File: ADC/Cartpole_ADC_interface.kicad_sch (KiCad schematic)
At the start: 9 parts, among them J1 Socket for JST XH, J2 Socket for potentiometer leads

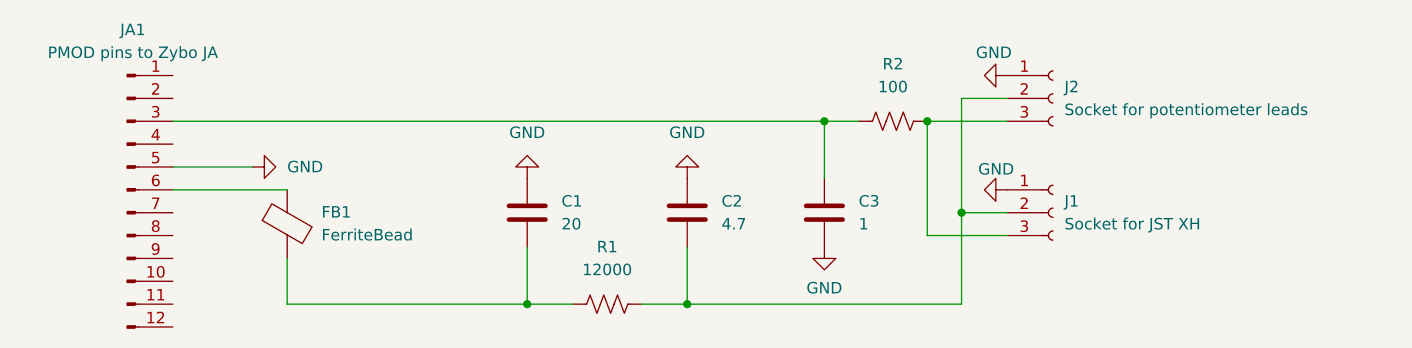
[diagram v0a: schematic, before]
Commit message: Fit left size of ADC interface board to the PMOD spec
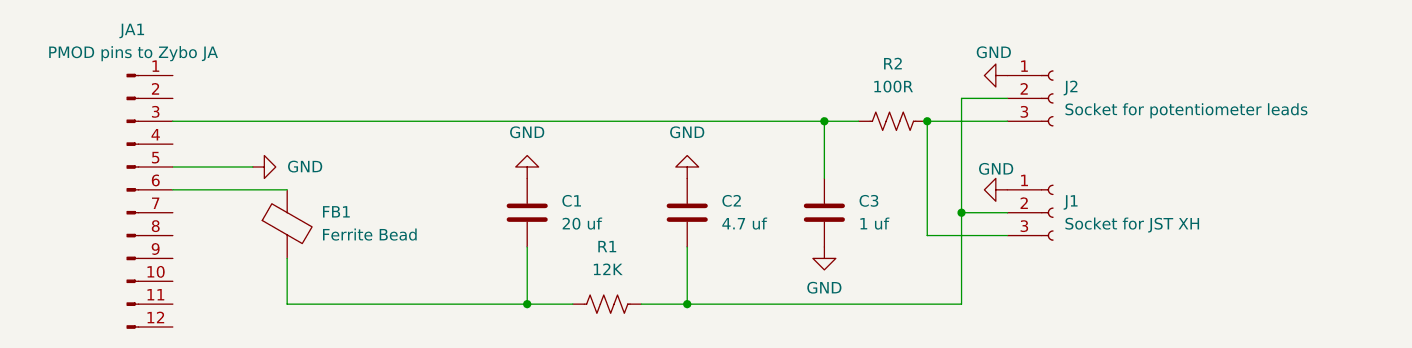
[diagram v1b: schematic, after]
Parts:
- C1: value 20 -> 20 uf
- C2: value 4.7 -> 4.7 uf
- C3: value 1 -> 1 uf
- FB1: value FerriteBead -> Ferrite Bead
- R1: value 12000 -> 12K
- R2: value 100 -> 100R
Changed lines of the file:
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@@
 			)
 		)
-		(property "Value" "4.7"
+		(property "Value" "4.7 uf"
 			(at 87.63 44.4499 0)
 			(effects
@@
 			)
 		)
-		(property "Value" "FerriteBead"
+		(property "Value" "Ferrite Bead"
 			(at 43.18 45.6691 0)
 			(effects
@@
 			)
 		)
-		(property "Value" "1"
+		(property "Value" "1 uf"
 			(at 102.87 44.4499 0)
 			(effects
@@
 			)
 		)
-		(property "Value" "100"
+		(property "Value" "100R"
 			(at 106.68 29.21 90)
 			(effects
@@
 			)
 		)
-		(property "Value" "20"
+		(property "Value" "20 uf"
 			(at 69.85 44.4499 0)
 			(effects
@@
 			)
 		)
-		(property "Value" "12000"
+		(property "Value" "12K"
 			(at 74.93 49.53 90)
 			(effects

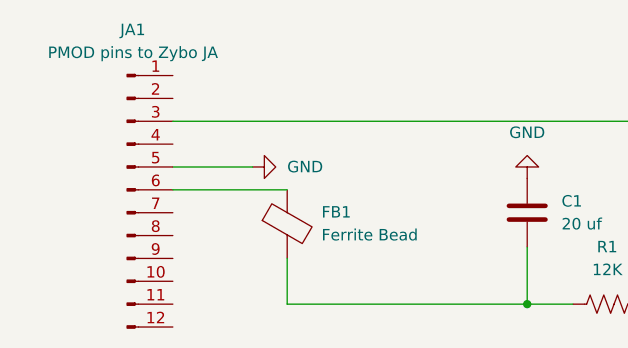
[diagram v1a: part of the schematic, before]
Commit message: Grounded pin 9 of the adc interface board (apparently this is atually necessary)
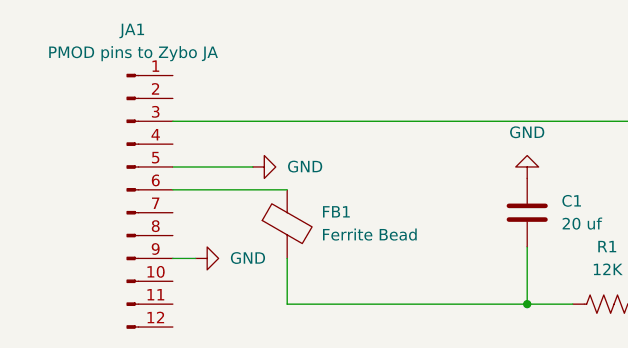
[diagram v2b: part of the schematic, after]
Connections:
- net GND: now also JA1.9 (Pin_9)
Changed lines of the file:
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@@
+	(wire
+		(pts
+			(xy 29.21 48.26) (xy 26.67 48.26)
+		)
+		(stroke
+			(width 0)
+			(type default)
+		)
+	)
 	(wire
 		(pts
@@
 					(unit 1)
 				)
+			)
+		)
+	)
+	(symbol
+		(lib_id "power:GND")
+		(at 29.21 48.26 90)
+		(unit 1)
+		(exclude_from_sim no)
+		(in_bom yes)
+		(on_board yes)
+		(dnp no)
+		(fields_autoplaced yes)
+		(property "Reference" "#PWR07"
+			(at 35.56 48.26 0)
+			(effects
+				(font
+					(size 1.27 1.27)
+				)
+				(hide yes)
+			)
+		)
+		(property "Value" "GND"
+			(at 33.02 48.2599 90)
+			(effects
+				(font
+					(size 1.27 1.27)
+				)
+				(justify right)
+			)
+		)
+		(property "Footprint" ""
+			(at 29.21 48.26 0)
+			(effects
+				(font
+					(size 1.27 1.27)
+				)
+				(hide yes)
+			)
+		)
+		(property "Datasheet" ""
+			(at 29.21 48.26 0)
+			(effects
+				(font
+					(size 1.27 1.27)
+				)
+				(hide yes)
+			)
+		)
+		(property "Description" "Power symbol creates a global label with name \"GND\" , ground"
+			(at 29.21 48.26 0)
+			(effects
+				(font
+					(size 1.27 1.27)
+				)
+				(hide yes)
+			)
+		)
+		(pin "1"
+		)
+		(instances
+			(project ""
+				(path "/fe0e78ba-5d72-44e5-b313-82ba40ab0f1a"
+					(reference "#PWR07")
+					(unit 1)
+				)
